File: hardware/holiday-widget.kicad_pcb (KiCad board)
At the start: 4 copper layers, 150 x 75 mm, 113 parts, among them J1 I2C, J2 UART, J3 SPI, J33 Conn_02x05_Odd_Even, J4 BATTERY POWER, J5 VDC POWER, J6 Conn_01x08, J7 Speaker, Q1 MMBT3906, Q2 MMBT3906, Q3 MMBT3906, Q4 MMBT3906, Q5 MMBT3906, Q6 MMBT3906, Q7 MMBT3906, Q8 MMBT3906, SW1 SW_Push, SW4 SW_Push, U1 STM32L072RBTx, U2 TPS61200DRC, U3 LIS3DH, U4 IMP23ABSU, U5 TMP102xxDRL, U6 VCNL_4020, U7 PAM8302AAD

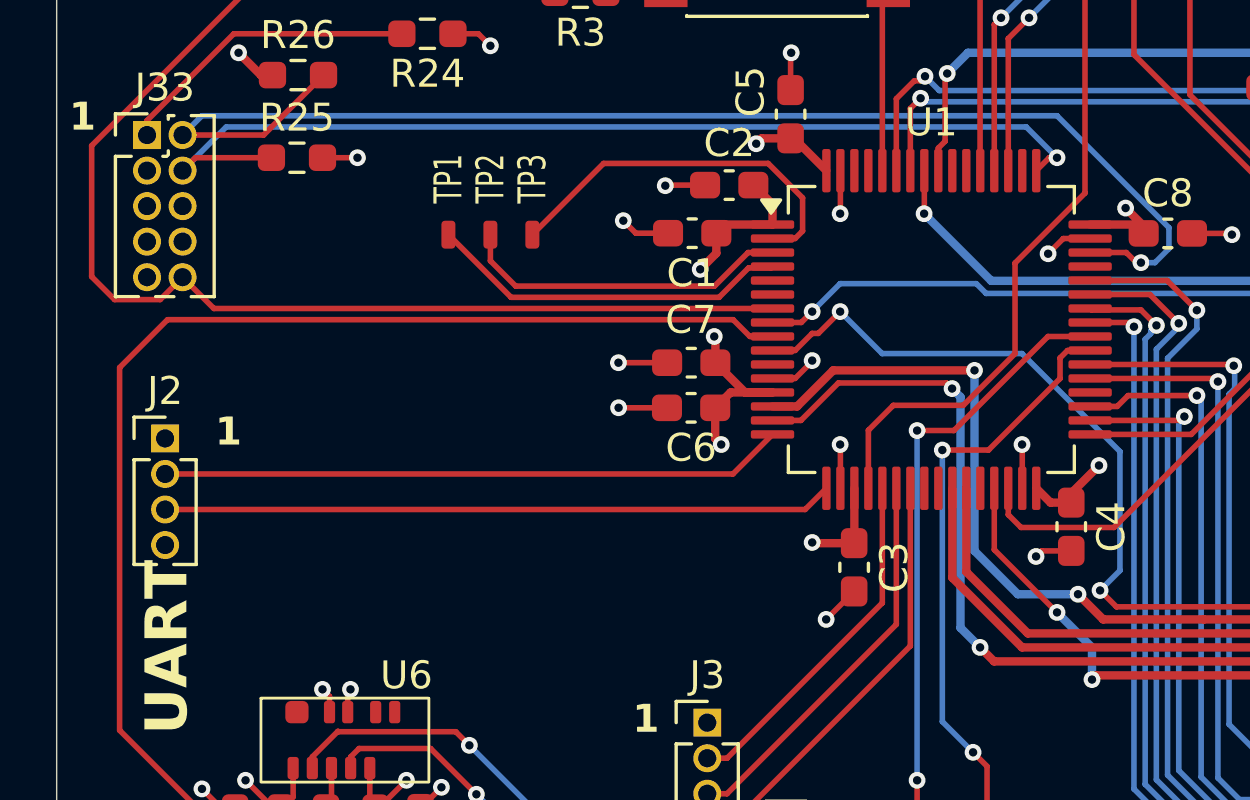
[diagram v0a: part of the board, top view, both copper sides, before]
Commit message: [Hardware] Update MCU pinout.
* Move UART RX to PA15
* Route audio input to PA3 in addition to PC0
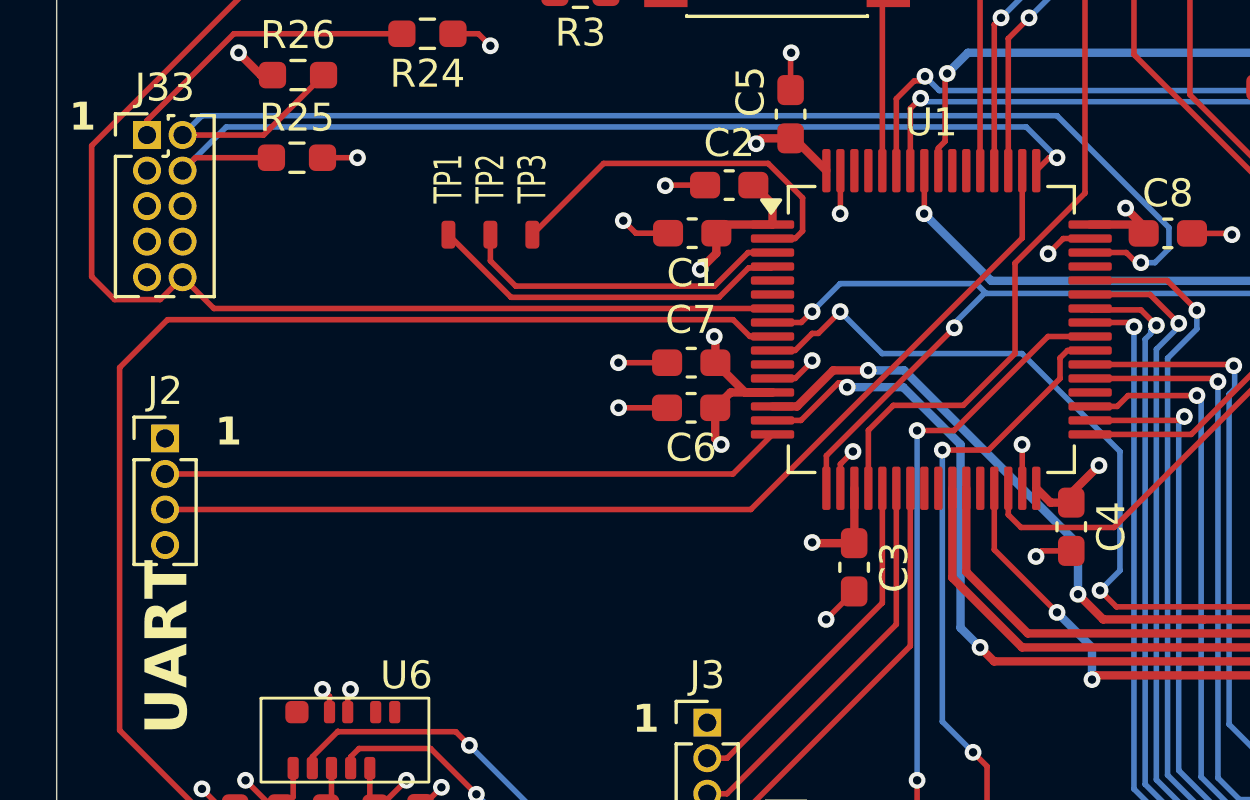
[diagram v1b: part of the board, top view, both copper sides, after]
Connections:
- U1 pad 17: /UART.RX -> /Sensors/AUDIO
- U1 pad 50: unconnected-(U1-PA15-Pad50) -> /UART.RX
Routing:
- net /UART.RX: track 23.9 -> 37.1 mm
- net /Sensors/AUDIO: track 59.0 -> 68.4 mm, vias 2 -> 3
- net /mcu/LED0: track 90.0 -> 87.2 mm
- net /mcu/LED1: track 48.1 -> 47.1 mm

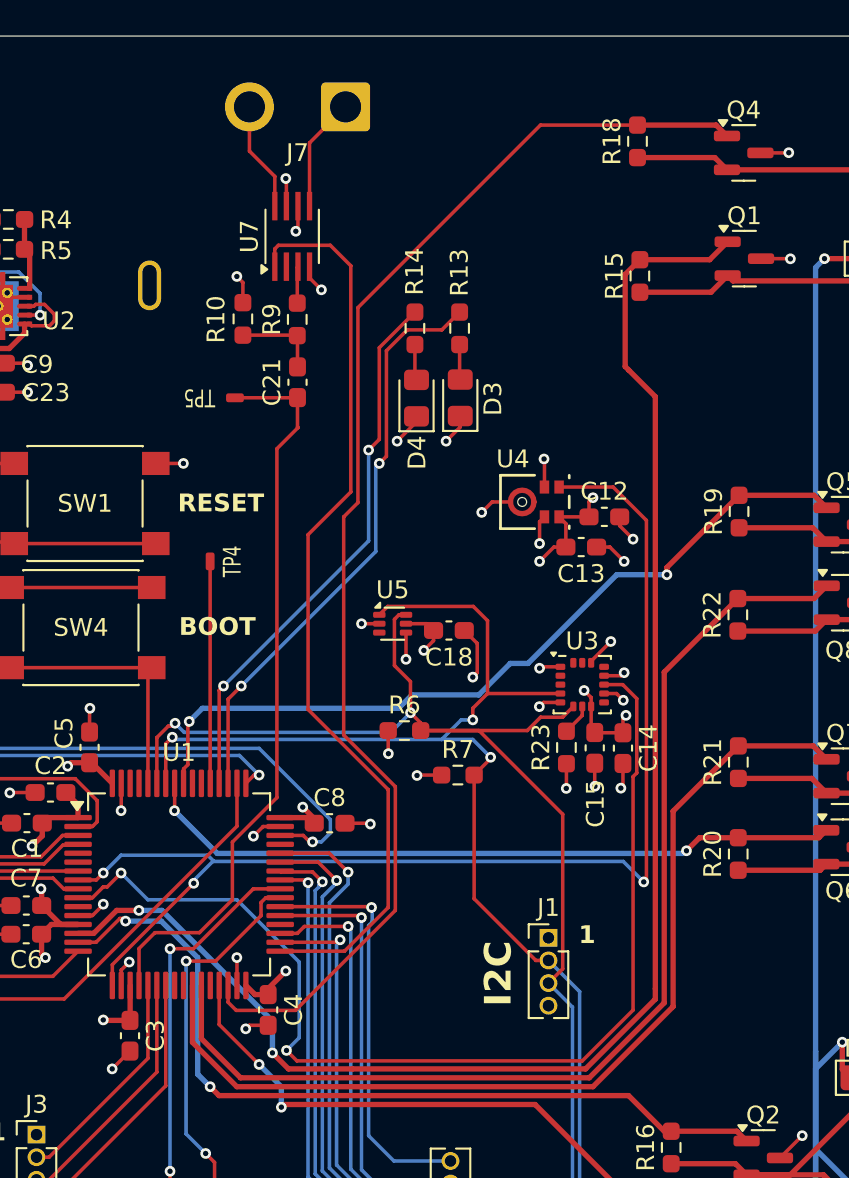
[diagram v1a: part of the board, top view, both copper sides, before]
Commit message: [Hardware] Add amplifier to microphone output.
The STM32 part we are using does not include an internal opamp, so we are adding an external opamp to bias and amplify the audio signal.

* Add opamp opa355
* calculate resistor network for gain of 10
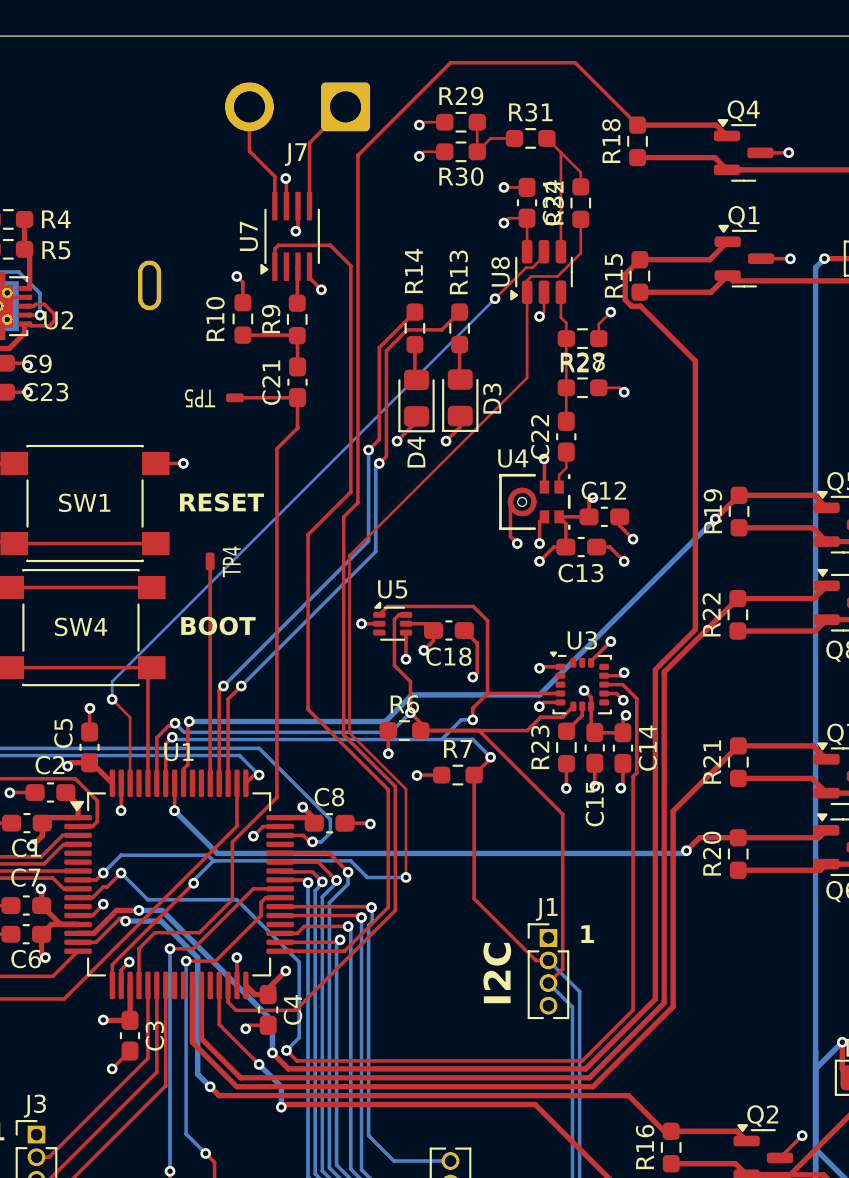
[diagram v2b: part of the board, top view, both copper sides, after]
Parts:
- added C22: 10u, Capacitor_SMD:C_0603_1608Metric_Pad1.08x0.95mm_HandSolder, F.Cu at (167.0, 94.0)
- added C24: 100n, Capacitor_SMD:C_0603_1608Metric_Pad1.08x0.95mm_HandSolder, F.Cu at (164.8, 80.9)
- added R27: 200k, Resistor_SMD:R_0603_1608Metric_Pad0.98x0.95mm_HandSolder, F.Cu at (167.9, 88.5)
- added R28: 200k, Resistor_SMD:R_0603_1608Metric_Pad0.98x0.95mm_HandSolder, F.Cu at (167.9, 91.2)
- added R29: 200k, Resistor_SMD:R_0603_1608Metric_Pad0.98x0.95mm_HandSolder, F.Cu at (161.1, 76.3)
- added R30: 200k, Resistor_SMD:R_0603_1608Metric_Pad0.98x0.95mm_HandSolder, F.Cu at (161.1, 78.0)
- added R31: 100k, Resistor_SMD:R_0603_1608Metric_Pad0.98x0.95mm_HandSolder, F.Cu at (165.0, 77.2)
- added R32: 1.8M, Resistor_SMD:R_0603_1608Metric_Pad0.98x0.95mm_HandSolder, F.Cu at (167.8, 80.9)
- added U8: OPA355NA, Package_TO_SOT_SMD:SOT-23-6, F.Cu at (165.8, 84.8)
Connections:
- U1 pad 17: /Sensors/AUDIO -> /Audio Amp/AUDIO_OUT
- U1 pad 62: unconnected-(U1-PB9-Pad62) -> /Audio Amp/AUDIO_AMP_EN
- U1 pad 8: /Sensors/AUDIO -> /Audio Amp/AUDIO_OUT
- U4 pad 1: /Sensors/AUDIO -> /Audio Amp/AUDIO_IN
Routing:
- net /Audio Amp/AUDIO_OUT: track 0.00 -> 73.4 mm, vias 0 -> 3
- net /Sensors/AUDIO: track 68.4 -> 0.00 mm, vias 3 -> 0
- net /Audio Amp/AUDIO_AMP_EN: track 0.00 -> 40.5 mm, vias 0 -> 2
- net Net-(U8--): track 0.00 -> 9.13 mm
- net /mcu/LED3: track 73.5 -> 81.4 mm
- net Net-(U8-+): track 0.00 -> 7.37 mm
- net /VDD: track 75.6 -> 82.2 mm, vias 29 -> 32
- net /GND: track 89.2 -> 95.7 mm, vias 56 -> 60
- net Net-(R29-Pad2): track 0.00 -> 4.06 mm
- net /mcu/LED0: track 87.2 -> 89.4 mm
- net /Audio Amp/AUDIO_IN: track 0.00 -> 2.13 mm

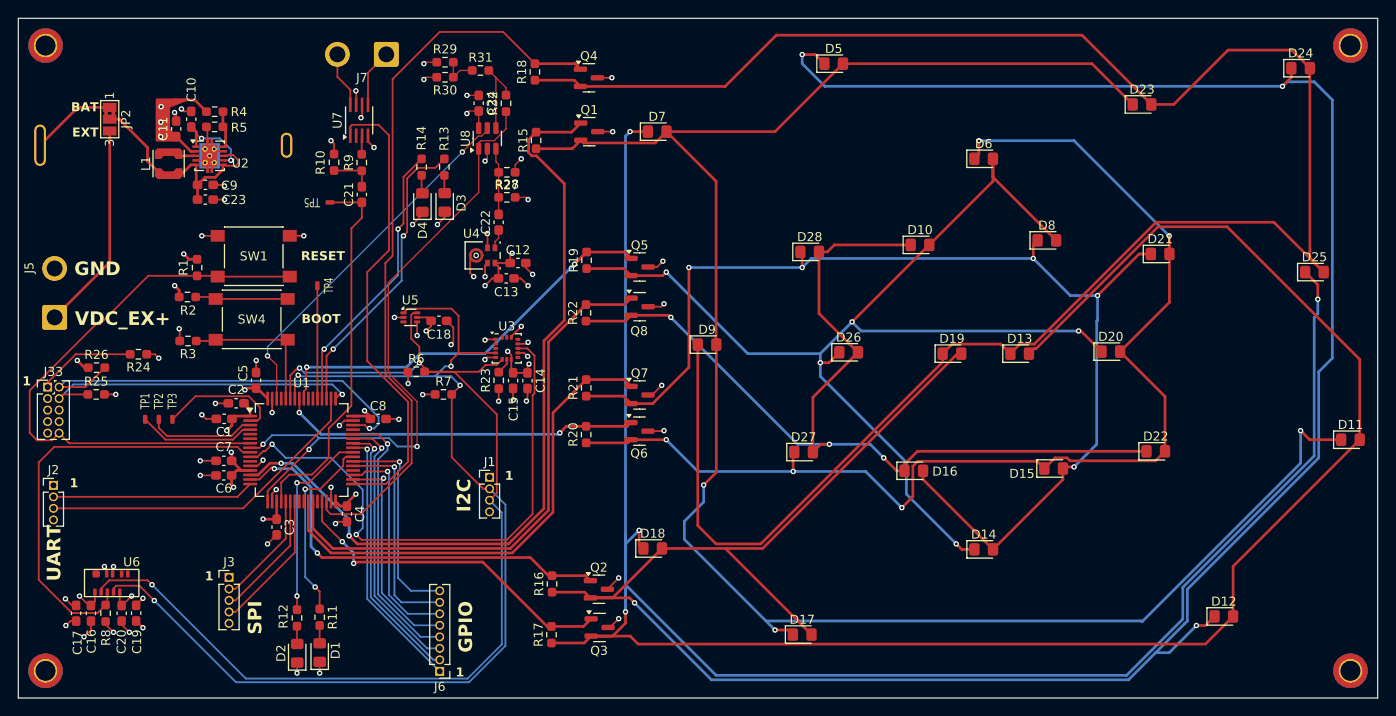
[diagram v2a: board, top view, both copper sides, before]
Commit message: [Hardware] Remove unused breakouts
* Remove extra GPIO and SPI outputs from MCU
* remove auxillary connectors for GPIO, SPI, and I2C
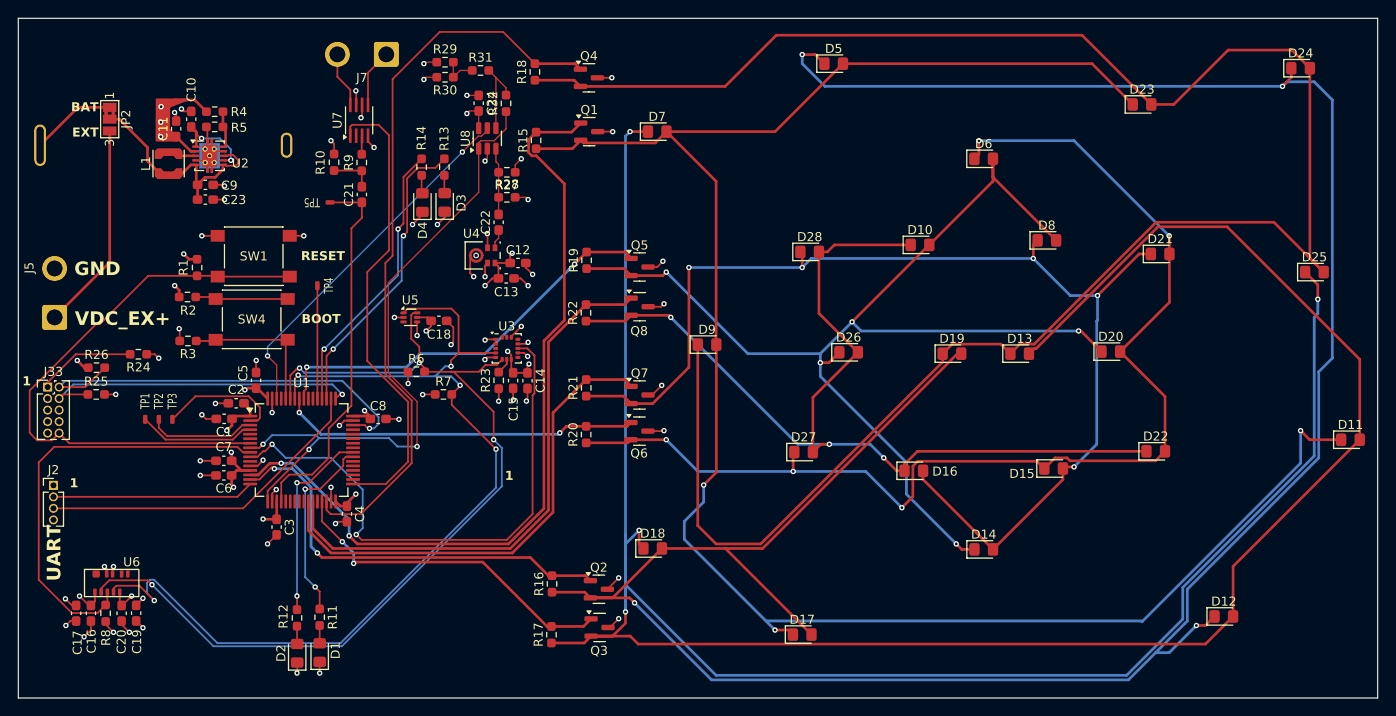
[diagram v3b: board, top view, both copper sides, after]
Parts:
- removed G***: LOGO, Leaf_Mechanical:leaf_logo_small
- removed J1: I2C, Connector_PinHeader_1.27mm:PinHeader_1x04_P1.27mm_Vertical
- removed J3: SPI, Connector_PinHeader_1.27mm:PinHeader_1x05_P1.27mm_Vertical
- removed J6: Conn_01x08, Connector_PinHeader_1.27mm:PinHeader_1x08_P1.27mm_Vertical
- removed REF** (x4): MountingHole_2.2mm_M2_DIN965_Pad_TopBottom, MountingHole:MountingHole_2.2mm_M2_DIN965_Pad_TopBottom
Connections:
- U1 pad 21: /SPI.SCK -> unconnected-(U1-PA5-Pad21)
- U1 pad 22: /SPI.DIN -> unconnected-(U1-PA6-Pad22)
- U1 pad 23: /SPI.DOUT -> unconnected-(U1-PA7-Pad23)
- U1 pad 34: /mcu/GPIO4 -> unconnected-(U1-PB13-Pad34)
- U1 pad 35: /mcu/GPIO5 -> unconnected-(U1-PB14-Pad35)
- U1 pad 37: /mcu/GPIO6 -> unconnected-(U1-PC6-Pad37)
- U1 pad 38: /mcu/GPIO7 -> unconnected-(U1-PC7-Pad38)
- U1 pad 41: /mcu/GPIO0 -> unconnected-(U1-PA8-Pad41)
- U1 pad 42: /mcu/GPIO1 -> unconnected-(U1-PA9-Pad42)
- U1 pad 43: /mcu/GPIO2 -> unconnected-(U1-PA10-Pad43)
- U1 pad 44: /mcu/GPIO3 -> unconnected-(U1-PA11-Pad44)
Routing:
- net /mcu/GPIO3: track 30.0 -> 0.00 mm, vias 1 -> 0
- net /mcu/GPIO2: track 29.8 -> 0.00 mm, vias 1 -> 0
- net /mcu/GPIO1: track 29.6 -> 0.00 mm, vias 1 -> 0
- net /mcu/GPIO0: track 29.5 -> 0.00 mm, vias 1 -> 0
- net /mcu/GPIO5: track 24.1 -> 0.00 mm, vias 1 -> 0
- net /mcu/GPIO6: track 24.1 -> 0.00 mm, vias 1 -> 0
- net /mcu/GPIO4: track 24.0 -> 0.00 mm, vias 1 -> 0
- net /mcu/GPIO7: track 23.3 -> 0.00 mm, vias 1 -> 0
- net /I2C.SDA: track 121.8 -> 105.0 mm, vias 3 -> 4
- net /SPI.DOUT: track 15.6 -> 0.00 mm
- net /SPI.DIN: track 14.1 -> 0.00 mm
- net /SPI.SCK: track 12.7 -> 0.00 mm
- net /I2C.SCL: track 121.7 -> 110.2 mm, vias 4 -> 5
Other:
- board text removed: "GPIO"
- board text removed: "I2C"
- board text removed: "SPI"

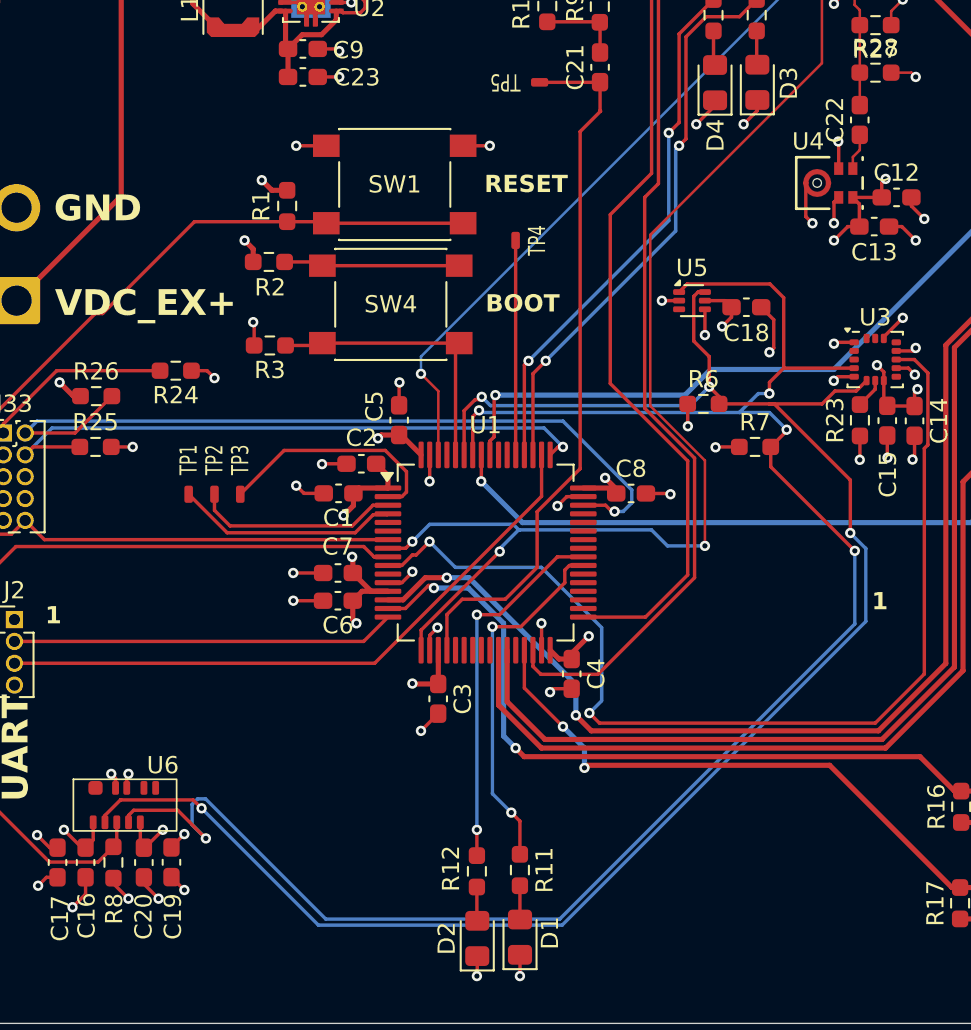
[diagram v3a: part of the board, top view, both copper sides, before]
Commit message: [Hardware] Update testpoints
* Add TPs for I2C since we removed the I2C header
* Add ground testpoints for GPIO and audio out
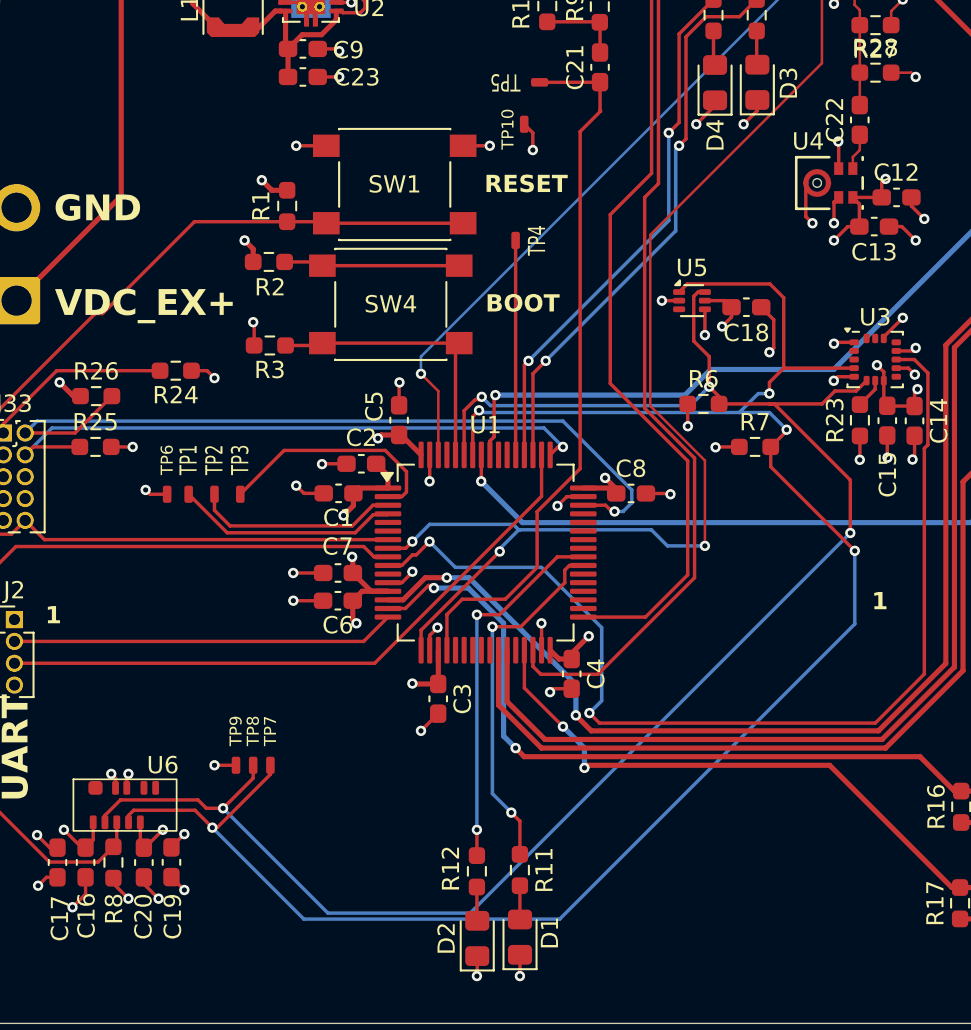
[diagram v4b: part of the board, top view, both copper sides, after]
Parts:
- added TP10: TestPoint, Leaf_Jumper:TestPoint_0.5mm_1mm, F.Cu at (147.5, 94.2)
- added TP6: TestPoint, Leaf_Jumper:TestPoint_0.5mm_1mm, F.Cu at (126.8, 115.8)
- added TP7: TestPoint, Leaf_Jumper:TestPoint_0.5mm_1mm, F.Cu at (132.8, 131.5)
- added TP8: TestPoint, Leaf_Jumper:TestPoint_0.5mm_1mm, F.Cu at (131.8, 131.5)
- added TP9: TestPoint, Leaf_Jumper:TestPoint_0.5mm_1mm, F.Cu at (130.8, 131.5)
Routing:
- net /GND: track 95.7 -> 100.0 mm, vias 60 -> 63
- net /I2C.SDA: track 105.0 -> 103.4 mm
- net /I2C.SCL: track 110.2 -> 111.2 mm
